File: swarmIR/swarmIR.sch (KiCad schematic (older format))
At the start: 18 parts, among them P1 CONN_2, P2 CONN_6, P3 CONN_2, P4 CONN_6, Q1 MOSFET_N, U1 TSOP1838, U2 TSOP1838, U3 TSOP1838, U4 TSOP1838

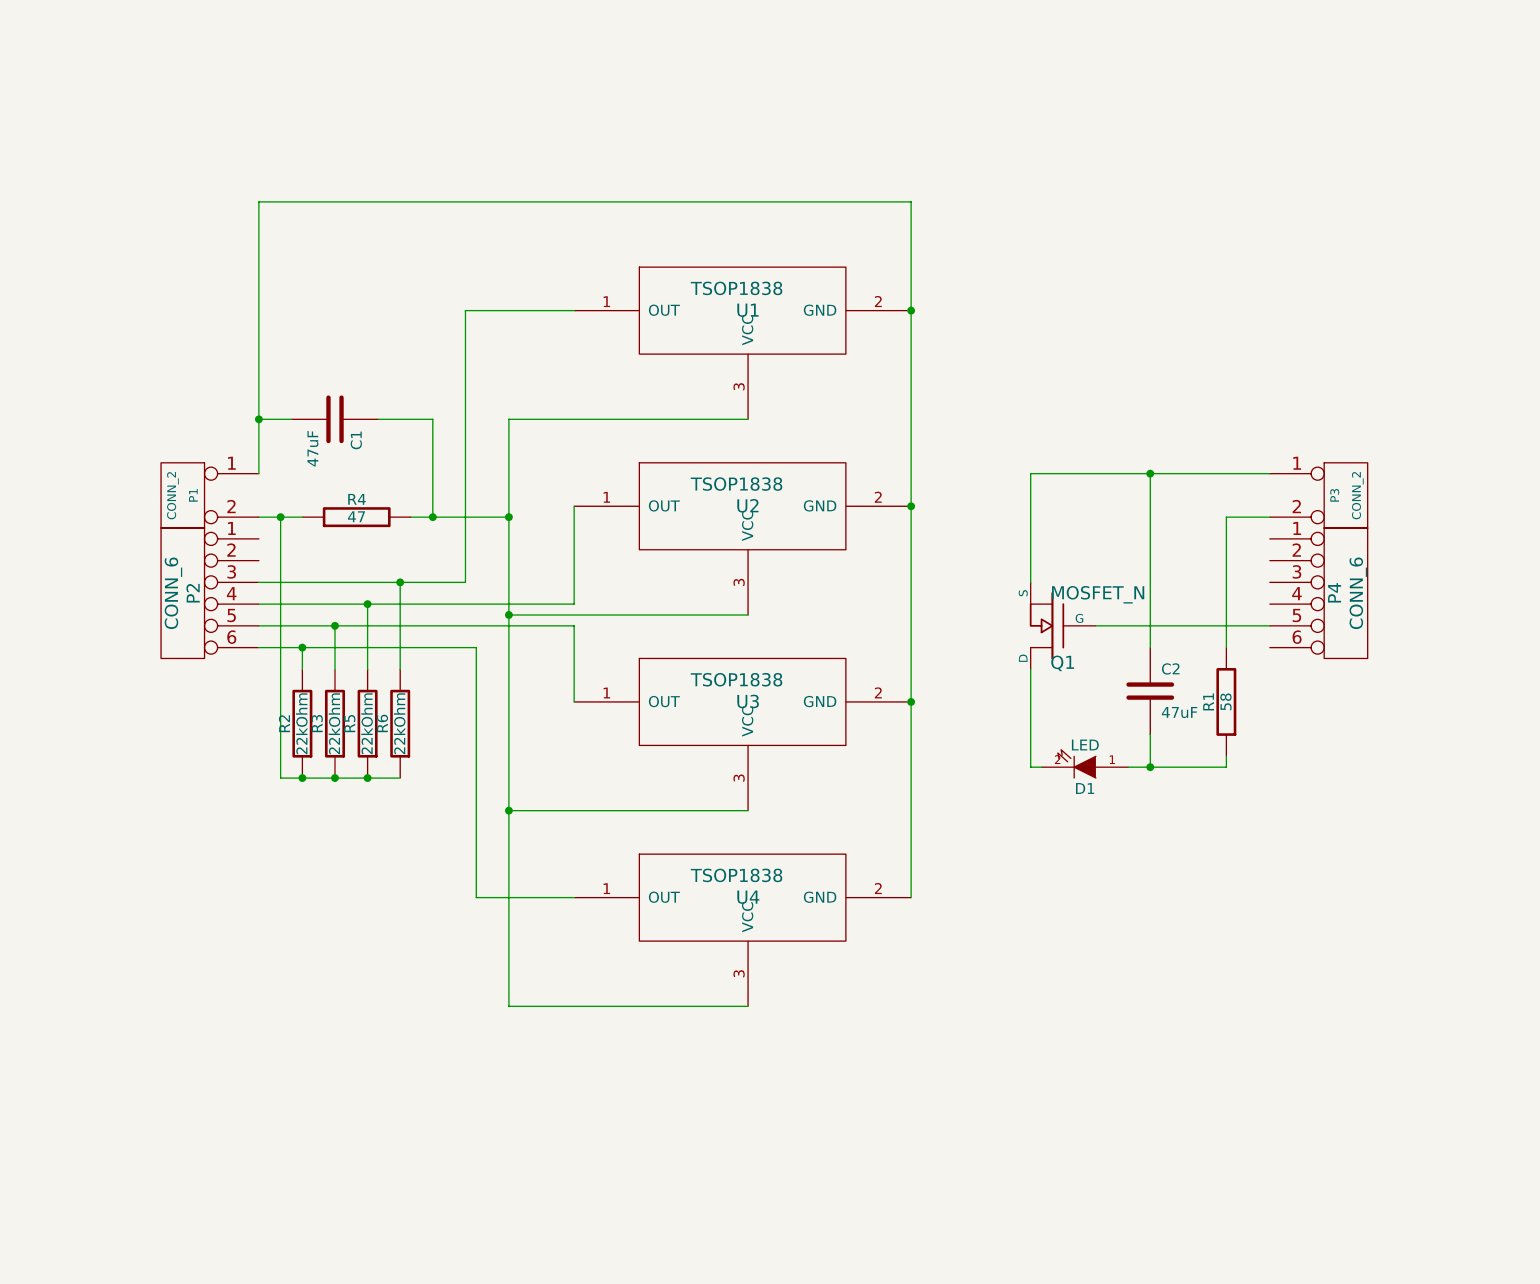
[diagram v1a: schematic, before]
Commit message: added 2 more IR Rx & pullups
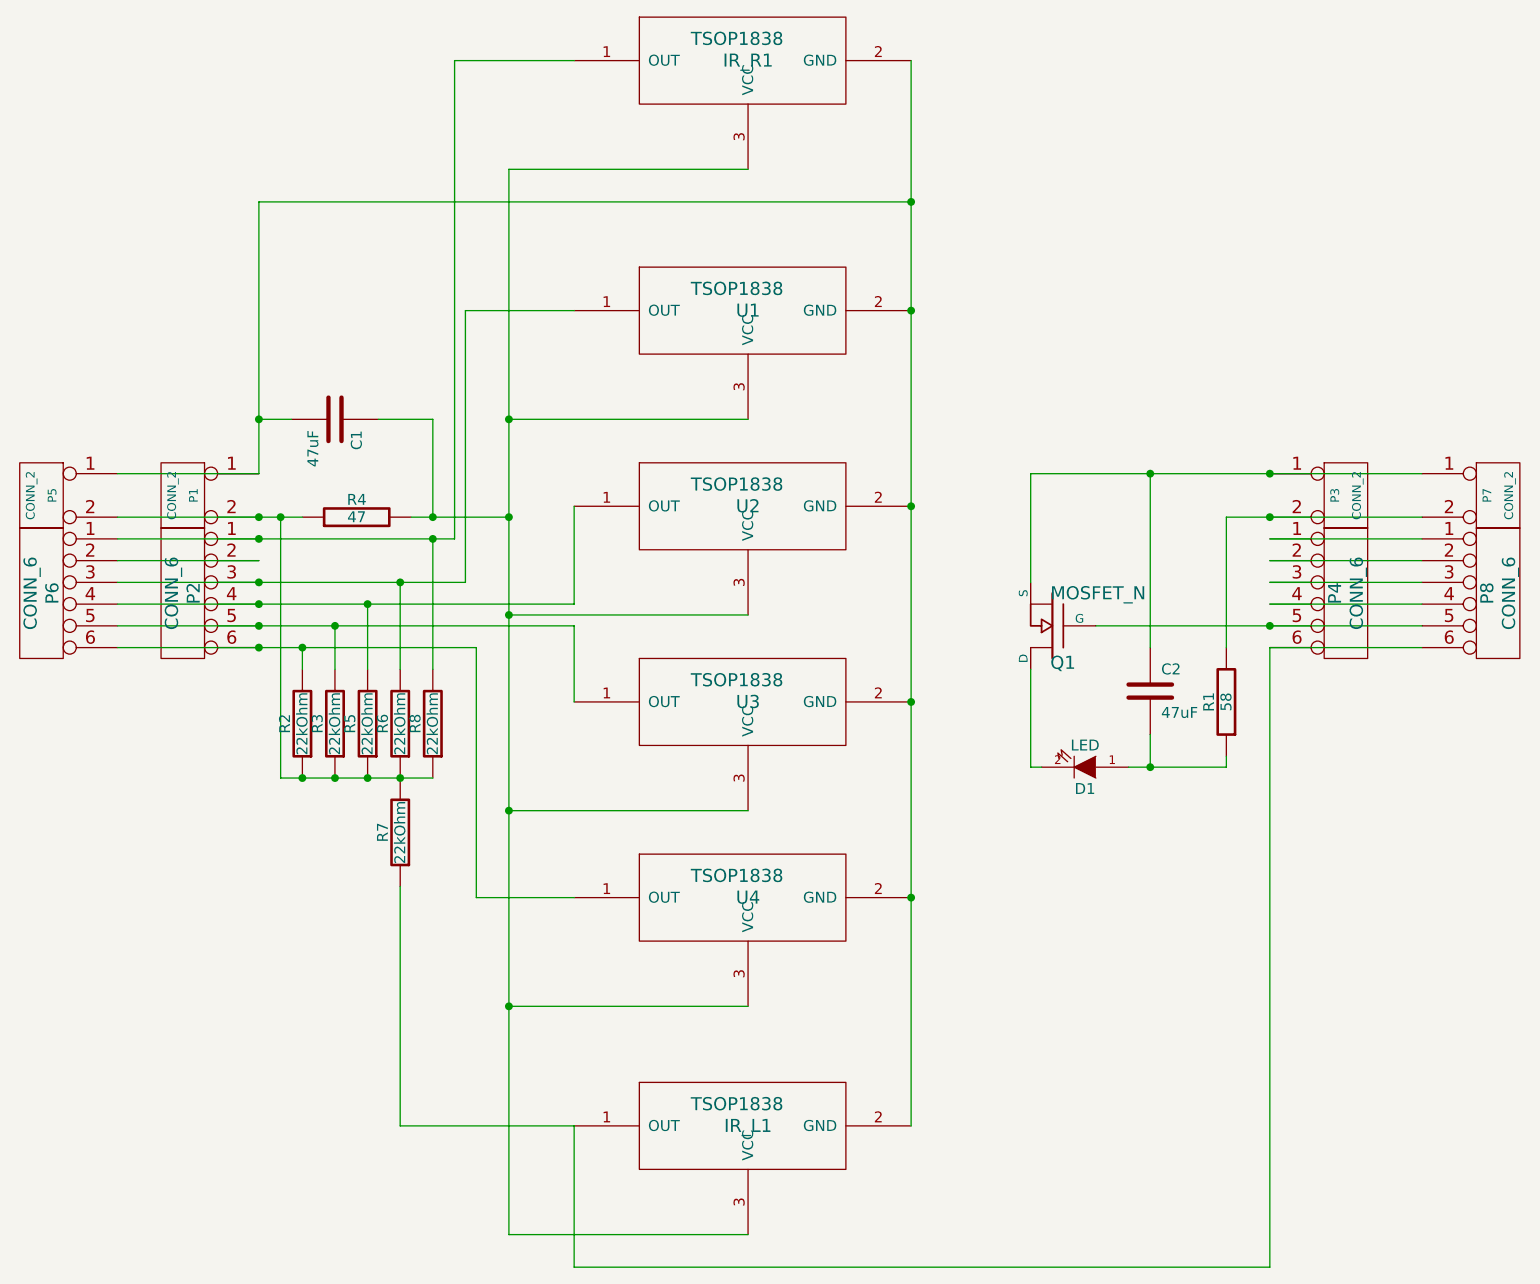
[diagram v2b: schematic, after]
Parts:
- added IR_L1, IR_R1: TSOP1838, symbol TSOP1838
- added P5, P7: CONN_2, symbol CONN_2
- added P6, P8: CONN_6, symbol CONN_6
- added R7, R8: 22kOhm, symbol R
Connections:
- net at P2.3, R6.2, U1.1 (OUT): now also P6.3
- net at C1.2, P1.1 (P1), U1.2 (GND)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: now also IR_L1.2 (GND), IR_R1.2 (GND), P5.1 (P1)
- net at C1.1, R4.2, U1.3 (VCC)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: now also IR_L1.3 (VCC), IR_R1.3 (VCC)
- net at P2.6, R2.2, U4.1 (OUT): now also P6.6
- net at P2.4, R5.2, U2.1 (OUT): now also P6.4
- net at P2.5, R3.2, U3.1 (OUT): now also P6.5
- net at P3.2 (PM), R1.2: now also P7.2 (PM)
- net at P4.5, Q1.G: now also P8.5
- net at C2.1, P3.1 (P1), Q1.S: now also P7.1 (P1)
- net at P1.2 (PM), R2.1, R3.1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: now also P5.2 (PM), R7.2, R8.1
- net at P2.1: now also IR_R1.1 (OUT), P6.1, R8.2
- net at P2.2: now also P6.2
- net at P4.1: now also P8.1
- net at P4.2: now also P8.2
- net at P4.3: now also P8.3
- net at P4.4: now also P8.4
- net at P4.6: now also IR_L1.1 (OUT), P8.6, R7.1
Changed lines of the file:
@@
-EESchema Schematic File Version 2  date Fri 12 Oct 2012 10:54:19 CST
+EESchema Schematic File Version 2  date Fri 12 Oct 2012 20:27:40 CST
 LIBS:power
 LIBS:device
@@
 	-1   0    0    1
 $EndComp
+$Comp
+L CONN_2 P7
+U 1 1 50780889
+P 8550 3200
+F 0 "P7" V 8500 3200 40  0000 C CNN
+F 1 "CONN_2" V 8600 3200 40  0000 C CNN
+	1    8550 3200
+	1    0    0    -1
+$EndComp
+$Comp
+L CONN_2 P5
+U 1 1 50780898
+P 1850 3200
+F 0 "P5" V 1800 3200 40  0000 C CNN
+F 1 "CONN_2" V 1900 3200 40  0000 C CNN
+	1    1850 3200
+	-1   0    0    -1
+$EndComp
+$Comp
+L CONN_6 P8
+U 1 1 507808BB
+P 8550 3650
+F 0 "P8" V 8500 3650 60  0000 C CNN
+F 1 "CONN_6" V 8600 3650 60  0000 C CNN
+	1    8550 3650
+	1    0    0    -1
+$EndComp
+$Comp
+L CONN_6 P6
+U 1 1 507808CA
+P 1850 3650
+F 0 "P6" V 1800 3650 60  0000 C CNN
+F 1 "CONN_6" V 1900 3650 60  0000 C CNN
+	1    1850 3650
+	-1   0    0    -1
+$EndComp
 Connection ~ 5850 3250
 Connection ~ 5850 4150
@@
 	5100 2850 4000 2850
 Wire Wire Line
-	4000 2850 4000 5550
+	4000 1700 4000 6600
 Wire Wire Line
 	3550 3300 4000 3300
@@
 	3800 2350 3800 3600
 Wire Wire Line
-	3800 3600 2850 3600
-Wire Wire Line
-	2850 3700 4300 3700
+	3800 3600 2200 3600
+Wire Wire Line
+	2200 3700 4300 3700
 Wire Wire Line
 	4300 3800 4300 4150
 Wire Wire Line
-	2850 3800 4300 3800
+	2200 3800 4300 3800
 Wire Wire Line
 	3850 5050 3850 3900
 Wire Wire Line
-	3850 3900 2850 3900
-Wire Wire Line
-	7500 3800 6700 3800
+	3850 3900 2200 3900
+Wire Wire Line
+	6700 3800 8200 3800
 Wire Wire Line
 	6400 3100 6400 3600
 Wire Wire Line
-	6400 3100 7500 3100
-Wire Wire Line
-	5850 1850 5850 5050
+	6400 3100 8200 3100
+Wire Wire Line
+	5850 1200 5850 6100
 Wire Wire Line
 	5850 1850 2850 1850
@@
 	2850 1850 2850 3100
 Wire Wire Line
-	3050 3300 2850 3300
+	2200 3300 3050 3300
 Wire Wire Line
 	3400 2850 3650 2850
@@
 Connection ~ 2850 2850
 Wire Wire Line
-	7500 3300 7300 3300
+	7300 3300 8200 3300
 Wire Wire Line
 	7300 3300 7300 3900
@@
 Connection ~ 6950 4450
 Wire Wire Line
-	2950 4500 3500 4500
+	2950 4500 3650 4500
 Connection ~ 3350 4500
 Connection ~ 3200 4500
@@
 	3500 4000 3500 3600
 Connection ~ 3500 3600
+Connection ~ 7500 3100
+Connection ~ 7500 3300
+Wire Wire Line
+	7500 3400 8200 3400
+Wire Wire Line
+	8200 3500 7500 3500
+Wire Wire Line
+	7500 3600 8200 3600
+Wire Wire Line
+	8200 3700 7500 3700
+Connection ~ 7500 3800
+Wire Wire Line
+	8200 3900 7500 3900
+Connection ~ 2850 3900
+Connection ~ 2850 3800
+Connection ~ 2850 3700
+Connection ~ 2850 3600
+Wire Wire Line
+	2200 3500 2850 3500
+Wire Wire Line
+	2200 3400 3750 3400
+Connection ~ 2850 3300
+Wire Wire Line
+	2850 3100 2200 3100
+$Comp
+L TSOP1838 IR_R1
+U 1 1 50780B0D
+P 5100 1200
+F 0 "IR_R1" H 5100 1200 60  0000 C CNN
+F 1 "TSOP1838" H 5050 1300 60  0000 C CNN
+	1    5100 1200
+	1    0    0    -1
+$EndComp
+$Comp
+L TSOP1838 IR_L1
+U 1 1 50780B13
+P 5100 6100
+F 0 "IR_L1" H 5100 6100 60  0000 C CNN
+F 1 "TSOP1838" H 5050 6200 60  0000 C CNN
+	1    5100 6100
+	1    0    0    -1
+$EndComp
+Connection ~ 5850 1850
+Wire Wire Line
+	5100 1700 4000 1700
+Connection ~ 4000 2850
+Connection ~ 5850 5050
+Wire Wire Line
+	4000 6600 5100 6600
+Connection ~ 4000 5550
+Wire Wire Line
+	7500 3900 7500 6750
+Wire Wire Line
+	7500 6750 4300 6750
+Wire Wire Line
+	4300 6750 4300 6100
+$Comp
+L R R7
+U 1 1 50780DF4
+P 3500 4750
+F 0 "R7" V 3580 4750 50  0000 C CNN
+F 1 "22kOhm" V 3500 4750 50  0000 C CNN
+	1    3500 4750
+	-1   0    0    1
+$EndComp
+Wire Wire Line
+	3500 5000 3500 6100
+Wire Wire Line
+	3500 6100 4300 6100
+$Comp
+L R R8
+U 1 1 50780EA2
+P 3650 4250
+F 0 "R8" V 3730 4250 50  0000 C CNN
+F 1 "22kOhm" V 3650 4250 50  0000 C CNN
+	1    3650 4250
+	-1   0    0    1
+$EndComp
+Connection ~ 3500 4500
+Wire Wire Line
+	4300 1200 3750 1200
+Wire Wire Line
+	3750 1200 3750 3400
+Connection ~ 2850 3400
+Wire Wire Line
+	3650 4000 3650 3400
+Connection ~ 3650 3400
 $EndSCHEMATC
